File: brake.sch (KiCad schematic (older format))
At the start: 10 parts, among them U6 INA180A, U7 A4953_LJ

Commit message: これで発注
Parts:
- C16: footprint Capacitor_SMD:C_0805_2012Metric -> Capacitor_SMD:C_1206_3216Metric
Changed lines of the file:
@@
 F 0 "C16" H 2865 2396 50  0000 L CNN
 F 1 "1u" H 2865 2305 50  0000 L CNN
-F 2 "Capacitor_SMD:C_0805_2012Metric" H 2788 2200 50  0001 C CNN
+F 2 "Capacitor_SMD:C_1206_3216Metric" H 2788 2200 50  0001 C CNN
 F 3 "~" H 2750 2350 50  0001 C CNN
 	1    2750 2350

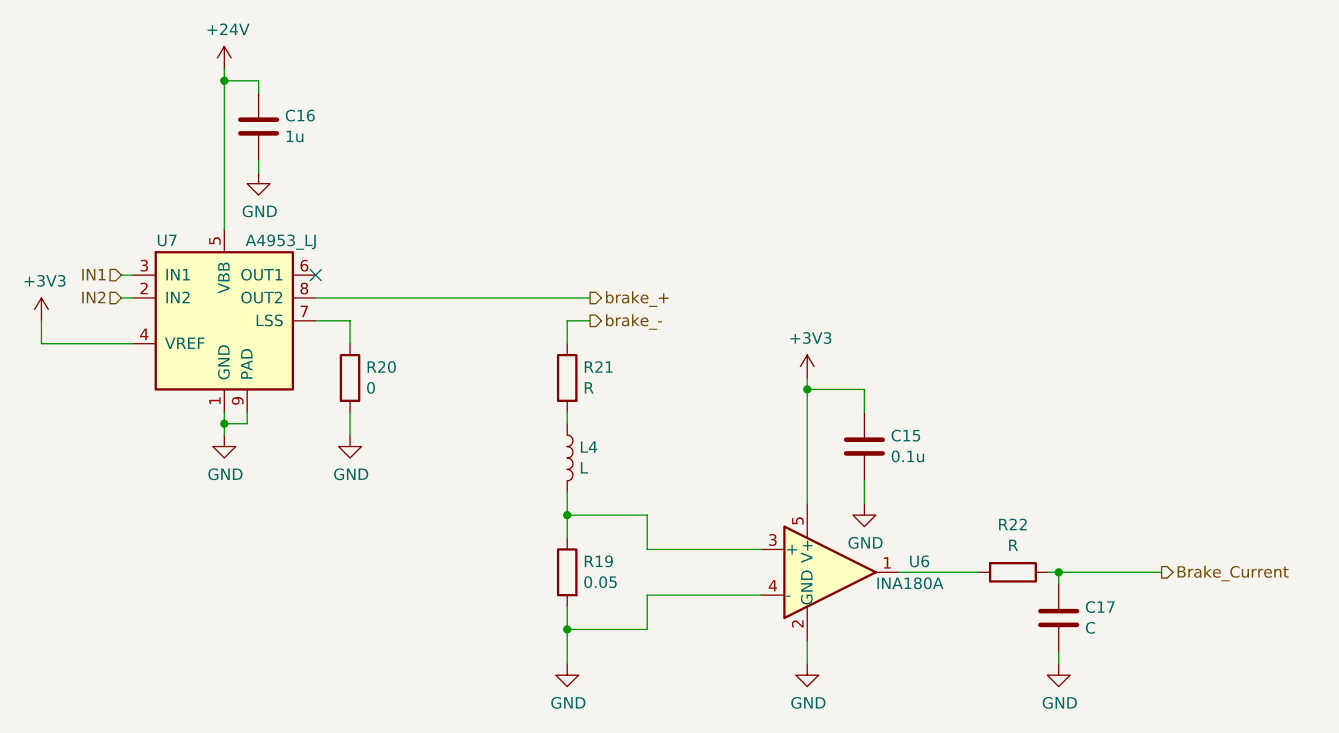
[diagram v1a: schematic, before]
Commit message: 見つけた設計ミスを全部反映
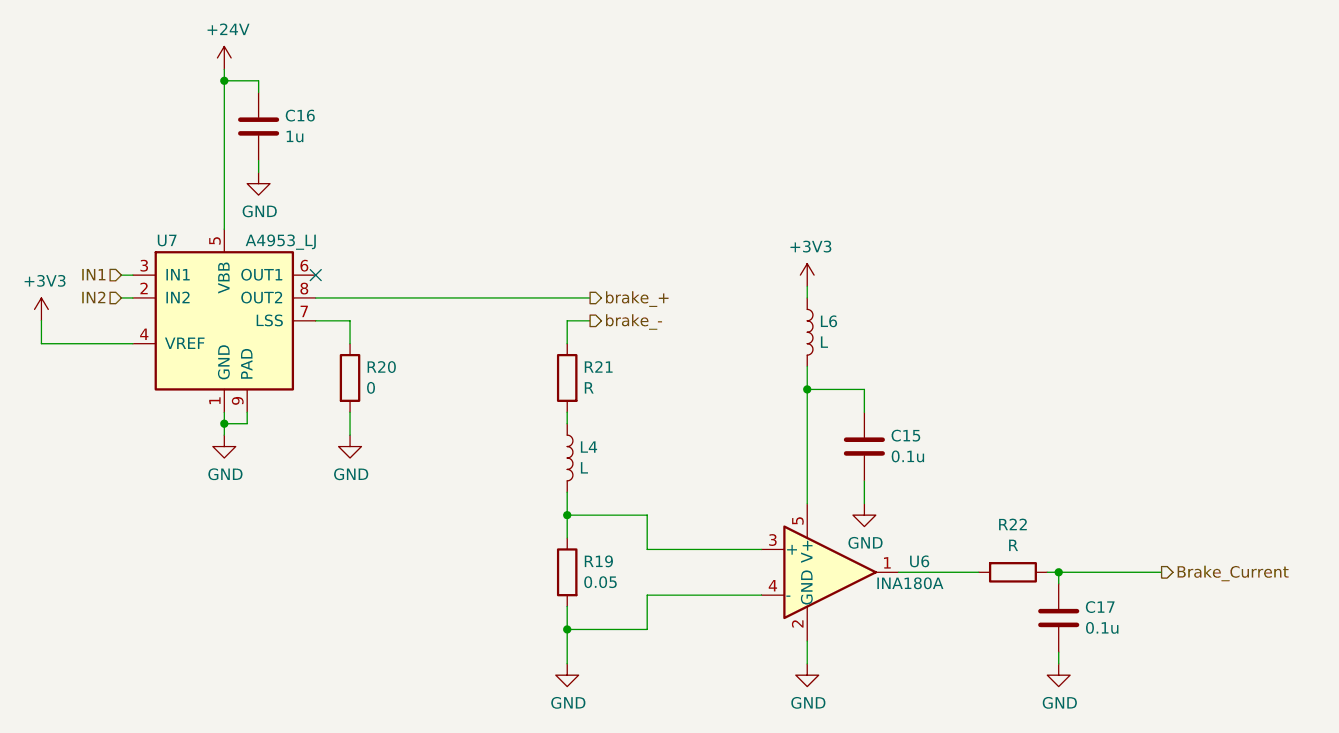
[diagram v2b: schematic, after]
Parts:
- added L6: L, Inductor_SMD:L_0603_1608Metric, symbol Device:L
- C17: value C -> 0.1u
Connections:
- net +3V3: now also L6.1; no longer C15.1, U6.5 (V+)
- new net: C15.1, L6.2, U6.5 (V+)
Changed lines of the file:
@@
 EESchema Schematic File Version 4
-LIBS:Encoder_check-cache
 EELAYER 30 0
 EELAYER END
@@
 L power:+3V3 #PWR0154
 U 1 1 5E52AC19
-P 5150 3450
-F 0 "#PWR0154" H 5150 3300 50  0001 C CNN
-F 1 "+3V3" H 5165 3623 50  0000 C CNN
-F 2 "" H 5150 3450 50  0001 C CNN
-F 3 "" H 5150 3450 50  0001 C CNN
-	1    5150 3450
-	1    0    0    -1
-$EndComp
-Wire Wire Line
-	5150 3450 5150 3500
+P 5150 3050
+F 0 "#PWR0154" H 5150 2900 50  0001 C CNN
+F 1 "+3V3" H 5165 3223 50  0000 C CNN
+F 2 "" H 5150 3050 50  0001 C CNN
+F 3 "" H 5150 3050 50  0001 C CNN
+	1    5150 3050
+	1    0    0    -1
+$EndComp
+Wire Wire Line
+	5150 3050 5150 3100
 Wire Wire Line
 	5150 3500 5400 3500
@@
 P 6250 4500
 F 0 "C17" H 6365 4546 50  0000 L CNN
-F 1 "C" H 6365 4455 50  0000 L CNN
+F 1 "0.1u" H 6365 4455 50  0000 L CNN
 F 2 "Capacitor_SMD:C_0603_1608Metric" H 6288 4350 50  0001 C CNN
 F 3 "~" H 6250 4500 50  0001 C CNN
@@
 Wire Wire Line
 	3000 3100 4200 3100
+$Comp
+L Device:L L6
+U 1 1 5E554509
+P 5150 3250
+F 0 "L6" H 5203 3296 50  0000 L CNN
+F 1 "L" H 5203 3205 50  0000 L CNN
+F 2 "Inductor_SMD:L_0603_1608Metric" H 5150 3250 50  0001 C CNN
+F 3 "~" H 5150 3250 50  0001 C CNN
+	1    5150 3250
+	1    0    0    -1
+$EndComp
+Wire Wire Line
+	5150 3400 5150 3500
 $EndSCHEMATC

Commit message: 部品のパラメータ未記入部分があったので追記
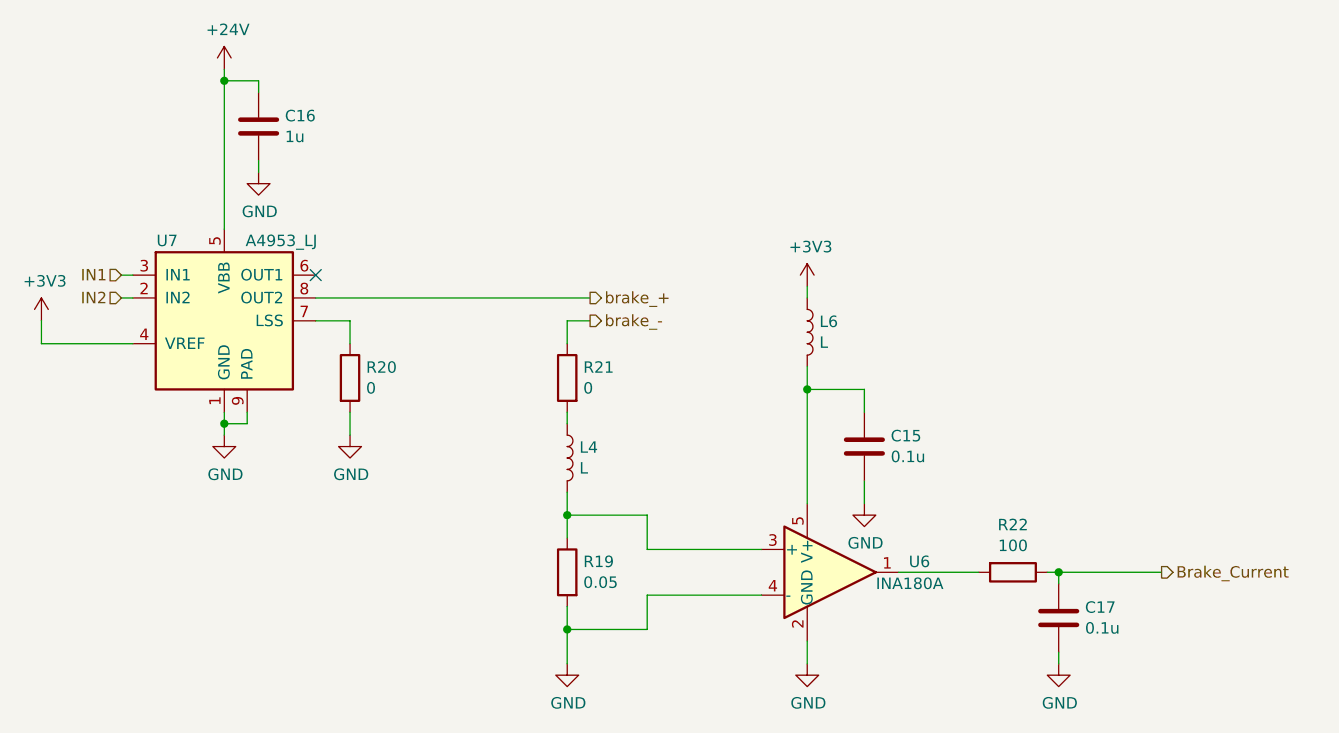
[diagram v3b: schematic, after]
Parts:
- R21: value R -> 0
- R22: value R -> 100
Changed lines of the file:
@@
 P 4100 3450
 F 0 "R21" H 4030 3496 50  0000 R CNN
-F 1 "R" H 4030 3405 50  0000 R CNN
+F 1 "0" H 4030 3405 50  0000 R CNN
 F 2 "Resistor_SMD:R_1206_3216Metric" V 4030 3450 50  0001 C CNN
 F 3 "~" H 4100 3450 50  0001 C CNN
@@
 P 6050 4300
 F 0 "R22" V 5843 4300 50  0000 C CNN
-F 1 "R" V 5934 4300 50  0000 C CNN
+F 1 "100" V 5934 4300 50  0000 C CNN
 F 2 "Inductor_SMD:L_0603_1608Metric" V 5980 4300 50  0001 C CNN
 F 3 "~" H 6050 4300 50  0001 C CNN

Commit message: 設計修正
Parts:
- removed R21: 0, Resistor_SMD:R_1206_3216Metric, symbol Device:R
- added L7: L, Inductor_SMD:L_1210_3225Metric, symbol Device:L
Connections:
- net brake_-: now also L7.1
- net at L4.1: now also L7.2
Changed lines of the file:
@@
 	4100 3650 4100 3600
-$Comp
-L Device:R R21
-U 1 1 5E5F967F
-P 4100 3450
-F 0 "R21" H 4030 3496 50  0000 R CNN
-F 1 "0" H 4030 3405 50  0000 R CNN
-F 2 "Resistor_SMD:R_1206_3216Metric" V 4030 3450 50  0001 C CNN
-F 3 "~" H 4100 3450 50  0001 C CNN
-	1    4100 3450
-	-1   0    0    -1
-$EndComp
 $Comp
 L Device:R R22
@@
 Wire Wire Line
 	5150 3400 5150 3500
+$Comp
+L Device:L L7
+U 1 1 5E86C289
+P 4100 3450
+F 0 "L7" H 4153 3496 50  0000 L CNN
+F 1 "L" H 4153 3405 50  0000 L CNN
+F 2 "Inductor_SMD:L_1210_3225Metric" H 4100 3450 50  0001 C CNN
+F 3 "~" H 4100 3450 50  0001 C CNN
+	1    4100 3450
+	1    0    0    -1
+$EndComp
 $EndSCHEMATC
